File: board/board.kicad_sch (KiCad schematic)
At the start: 2 parts, among them J1 013_PoE_rectified, J2 003_power

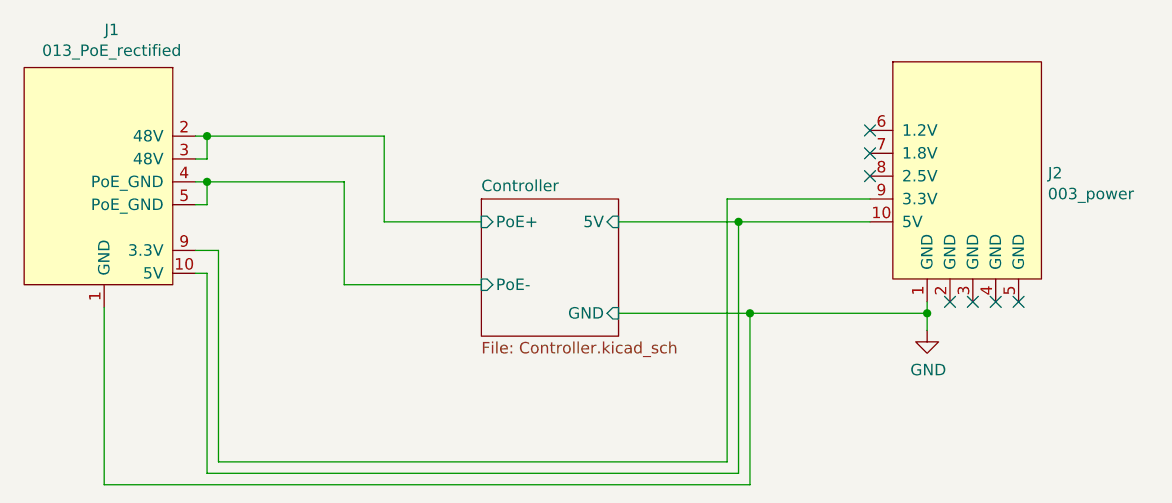
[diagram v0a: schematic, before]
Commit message: updated current limmit resistor
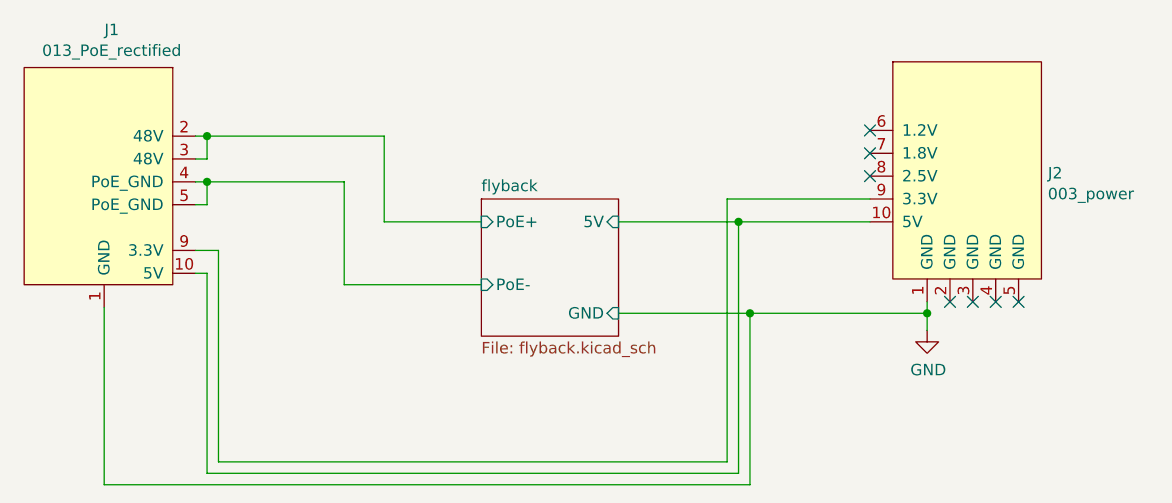
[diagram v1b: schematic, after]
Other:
- sheet Controller renamed flyback
- sheet flyback: file Controller.kicad_sch -> flyback.kicad_sch
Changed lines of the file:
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@@
     (stroke (width 0) (type solid) (color 0 0 0 0))
     (fill (color 0 0 0 0.0000))
-    (property "Sheet name" "Controller" (id 0) (at 129.54 83.1084 0)
+    (property "Sheet name" "flyback" (id 0) (at 129.54 83.1084 0)
       (effects (font (size 1.27 1.27)) (justify left bottom))
     )
-    (property "Sheet file" "Controller.kicad_sch" (id 1) (at 129.54 99.6446 0)
+    (property "Sheet file" "flyback.kicad_sch" (id 1) (at 129.54 99.6446 0)
       (effects (font (size 1.27 1.27)) (justify left top))
     )
@@
     )
     (path "/00000000-0000-0000-0000-00006083c3a8/00000000-0000-0000-0000-000060a2372f"
-      (reference "R5") (unit 1) (value "52.3k") (footprint "Resistor_SMD:R_0603_1608Metric")
+      (reference "R5") (unit 1) (value "64.9k") (footprint "Resistor_SMD:R_0603_1608Metric")
     )
     (path "/00000000-0000-0000-0000-00006083c3a8/00000000-0000-0000-0000-000060a12ead"
